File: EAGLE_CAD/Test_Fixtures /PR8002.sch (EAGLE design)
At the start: 29 parts, among them J1 M3_SCREW_POST, U1 V_REG_317SMD

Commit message: Updates to PR8002
Added RPI GPIO connections.
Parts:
- removed JP1, JP2: SMT/THJumper, SparkFun-Connectors:M02LOCK_LONGPADS
- removed TO_MCU: PINHD-1X10, adafruit:PINHD-1X10
- added LED2, LED3: (no value), adafruit:LEDCHIP-LED0805
- added R3: 1k, PR_Parts_Library:R_SMT_0805_ADAFRUIT
- added RPI_GPIO: M13X22X13, PR_Parts_Library:M13X22X13
- added U$20, U$22, U$23, U$24: C&K_PTS645, PR_Parts_Library:C&K_PTS645
- LED1: device adafruit:LED5MM -> adafruit:LEDCHIP-LED0805
- R1: value RV170SF_TAIWANA_POT_SW -> 1k; device PR_Parts_Library:RV170SF_TAIWANA_POT_SW -> PR_Parts_Library:R_SMT_0805_ADAFRUIT; MFG_PN RV170SF-43-20F-A10K - supplied by CL Labs -> (none)
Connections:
- removed net DUTPRES: TO_MCU.1, U$2.P$1
- removed net TSW: TO_MCU.4, U$9.P$1
- new net A_IN: U$17.P$1
- new net DEV_PRES: RPI_GPIO.GPIO3, U$2.P$1
- new net N$10: LED3.C, R3.2
- new net N$3: RPI_GPIO.GPIO8, U$20.P$1
- new net N$4: RPI_GPIO.GPIO12, U$23.P$1
- new net N$8: LED3.A, RPI_GPIO.GPIO23
- new net N$9: LED2.C, R1.2
- new net TACSW: RPI_GPIO.GPIO5, U$9.P$1
- net A_OUT: no longer JP1.1
- net GND: now also R1.1, R3.1, RPI_GPIO.GND, U$20.P$4, U$22.P$4, U$23.P$4, U$24.P$4; no longer R1.GND
- net N$5: now also RPI_GPIO.GPIO10, U$22.P$1; no longer JP2.1, R1.SIGNAL
- net N$6: now also RPI_GPIO.GPIO16, U$24.P$1; no longer JP1.2, R1.WIPER
- net N$7: now also LED2.A, RPI_GPIO.GPIO21; no longer JP2.2, U$17.P$1
- net SW_IN: now also RPI_GPIO.GPIO11; no longer TO_MCU.2
- net SW_OUT: now also RPI_GPIO.GPIO13; no longer TO_MCU.3
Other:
- note added: "Audio from FMIC"
- note added: "Fixture Input | Station Set Switches"
- note added: "Output from POT to Amp"
- note added: "PR8002, PR92X Test Fixture"
- note added: "Pass Fail Indication"
- note added: "RPI Connect"
- note added: "Verifies radio's LED"
- note removed: "MCU Connect"
- note removed: "NOTES: - PSU, connects via dc barrel jack to a 3.3 vreg. -MCU header connects to tactile switch; device present (ground pad), and the two poles of the switched potentiometer (when populated). -LED, connects to an external led on the test fixture. -Ext Speaker, connects to JST jack on the fixture. -Switched Pot, allows for volume control when testing SMT only boards. Uses shunt jumpers when fully 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"
- note removed: "POT"
- note removed: "PR9020 Test Fixture"
- moved on the sheet: CN1, ISP1, LED1, R2

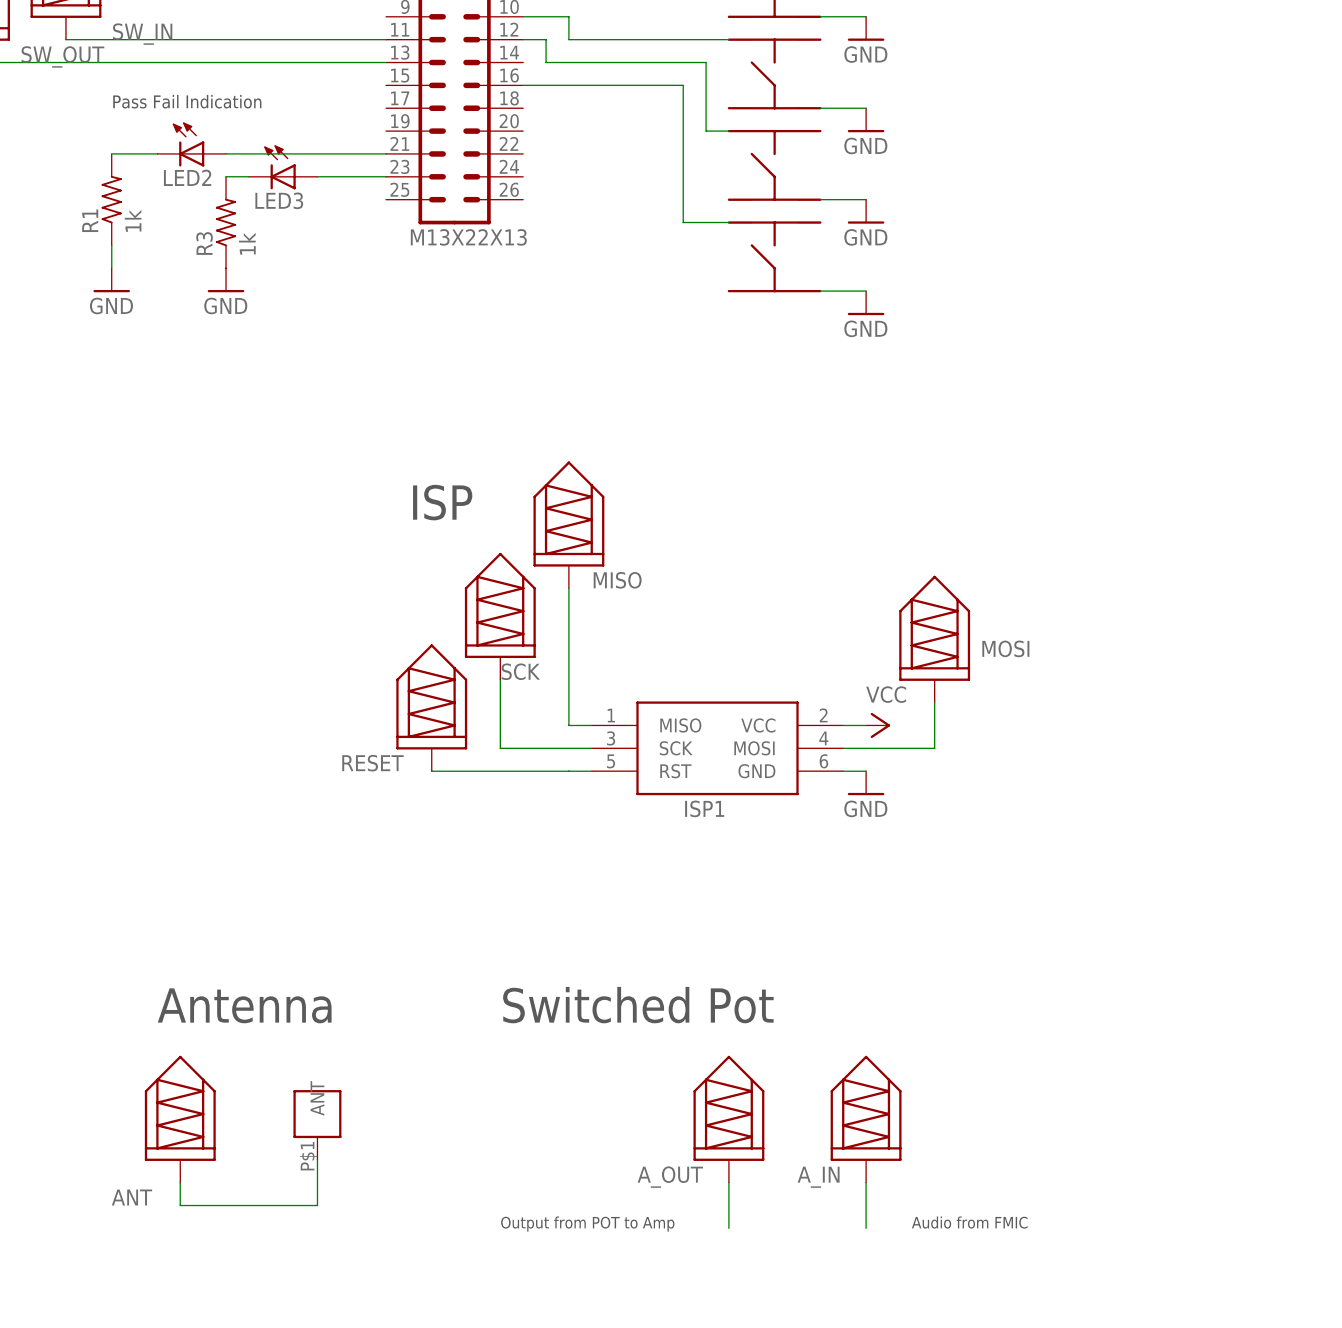
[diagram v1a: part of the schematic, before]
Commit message: PR8002 Updates
Progress on the Etest fixture schematic and layout
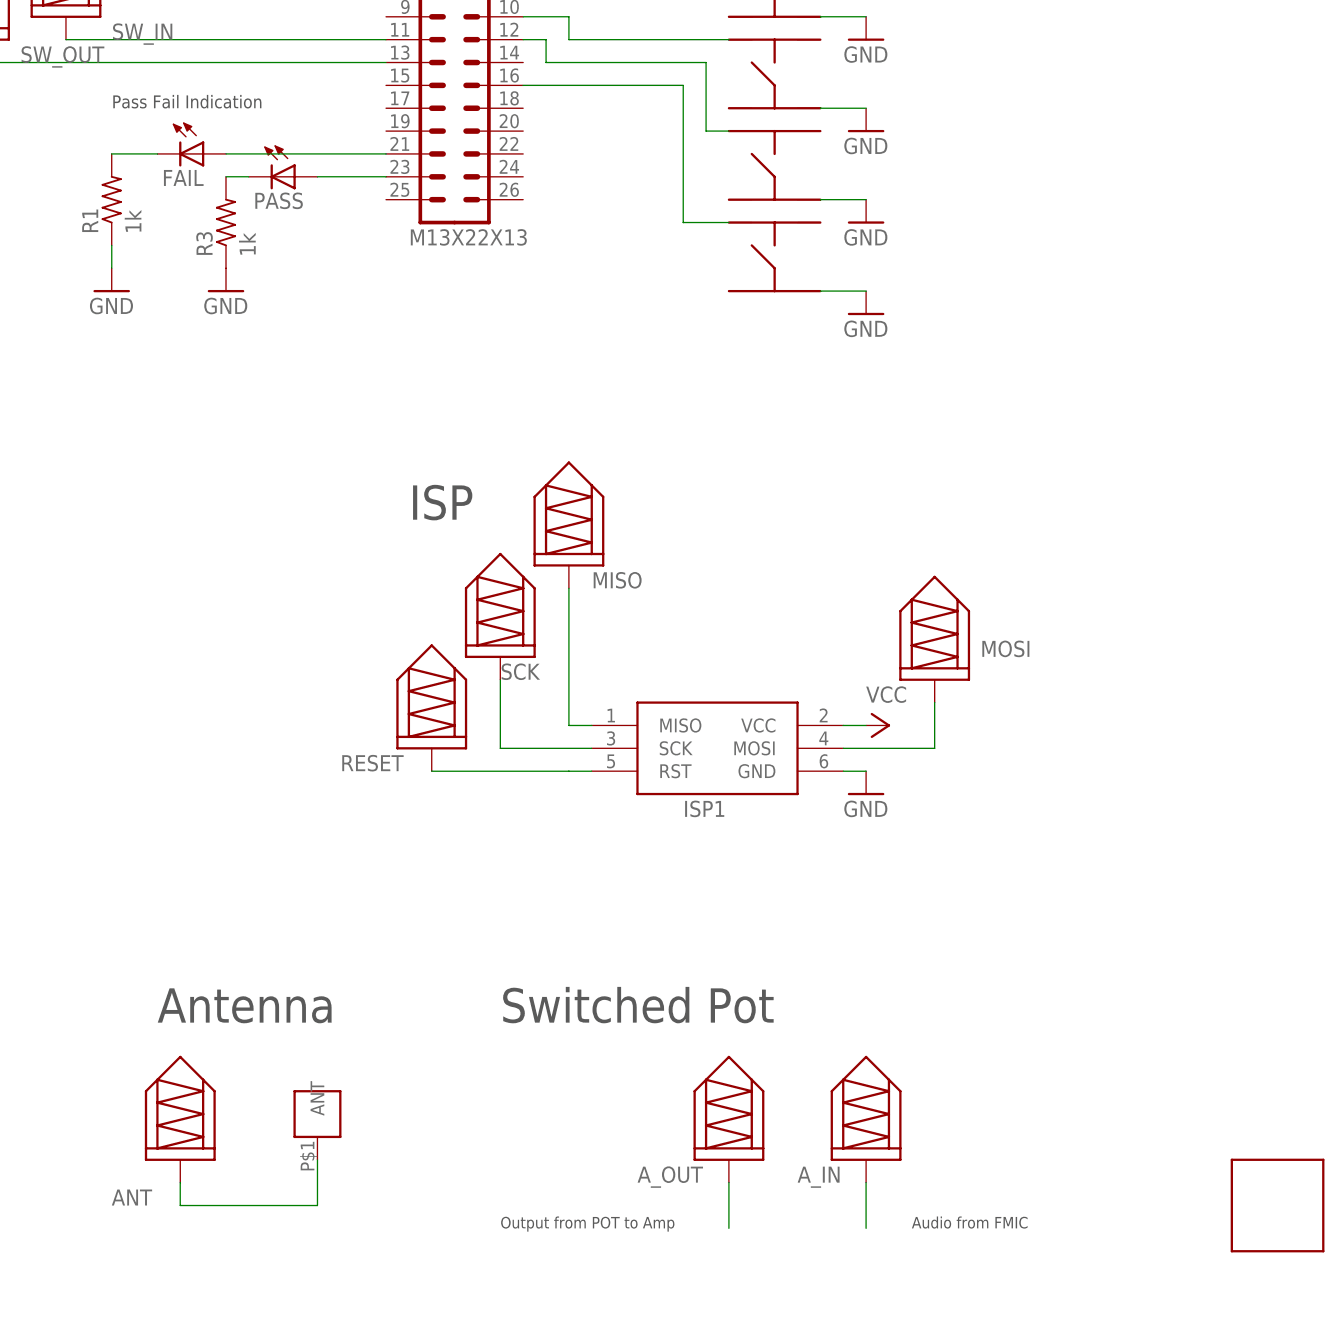
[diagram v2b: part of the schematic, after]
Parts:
- added U$25: SFUN_POCKETPROGRAMMER, PR_Parts_Library:SFUN_POCKETPROGRAMMER
- renumbered LED2 to FAIL, LED3 to PASS
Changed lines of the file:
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@@
 <part name="GND9" library="SparkFun-Aesthetics" deviceset="GND" device=""/>
 <part name="GND10" library="SparkFun-Aesthetics" deviceset="GND" device=""/>
-<part name="LED2" library="adafruit" deviceset="LED" device="CHIP-LED0805"/>
-<part name="LED3" library="adafruit" deviceset="LED" device="CHIP-LED0805"/>
+<part name="FAIL" library="adafruit" deviceset="LED" device="CHIP-LED0805"/>
+<part name="PASS" library="adafruit" deviceset="LED" device="CHIP-LED0805"/>
 <part name="R1" library="PR_Parts_Library" deviceset="R_SMT" device="_0805_ADAFRUIT" value="1k"/>
 <part name="R3" library="PR_Parts_Library" deviceset="R_SMT" device="_0805_ADAFRUIT" value="1k"/>
 <part name="GND11" library="SparkFun-Aesthetics" deviceset="GND" device=""/>
 <part name="GND12" library="SparkFun-Aesthetics" deviceset="GND" device=""/>
+<part name="U$25" library="PR_Parts_Library" deviceset="SFUN_POCKETPROGRAMMER" device=""/>
 </parts>
 <sheets>
@@
 <instance part="GND9" gate="1" x="205.74" y="106.68"/>
 <instance part="GND10" gate="1" x="205.74" y="96.52"/>
-<instance part="LED2" gate="G$1" x="132.08" y="114.3" rot="R270"/>
-<instance part="LED3" gate="G$1" x="142.24" y="111.76" rot="R270"/>
+<instance part="FAIL" gate="G$1" x="132.08" y="114.3" rot="R270"/>
+<instance part="PASS" gate="G$1" x="142.24" y="111.76" rot="R270"/>
 <instance part="R1" gate="G$1" x="121.92" y="109.22" rot="R90"/>
 <instance part="R3" gate="G$1" x="134.62" y="106.68" rot="R90"/>
 <instance part="GND11" gate="1" x="134.62" y="99.06"/>
 <instance part="GND12" gate="1" x="121.92" y="99.06"/>
+<instance part="U$25" gate="G$1" x="251.46" y="-2.54"/>
 </instances>
 <busses>
@@
 <segment>
 <pinref part="RPI_GPIO" gate="G$1" pin="GPIO21"/>
-<pinref part="LED2" gate="G$1" pin="A"/>
+<pinref part="FAIL" gate="G$1" pin="A"/>
 <wire x1="134.62" y1="114.3" x2="152.4" y2="114.3" width="0.1524" layer="91"/>
 </segment>
@@
 <segment>
 <pinref part="RPI_GPIO" gate="G$1" pin="GPIO23"/>
-<pinref part="LED3" gate="G$1" pin="A"/>
+<pinref part="PASS" gate="G$1" pin="A"/>
 <wire x1="144.78" y1="111.76" x2="152.4" y2="111.76" width="0.1524" layer="91"/>
 </segment>
@@
 <net name="N$9" class="0">
 <segment>
-<pinref part="LED2" gate="G$1" pin="C"/>
+<pinref part="FAIL" gate="G$1" pin="C"/>
 <pinref part="R1" gate="G$1" pin="2"/>
 <wire x1="121.92" y1="114.3" x2="127" y2="114.3" width="0.1524" layer="91"/>
@@
 <net name="N$10" class="0">
 <segment>
-<pinref part="LED3" gate="G$1" pin="C"/>
+<pinref part="PASS" gate="G$1" pin="C"/>
 <pinref part="R3" gate="G$1" pin="2"/>
 <wire x1="134.62" y1="111.76" x2="137.16" y2="111.76" width="0.1524" layer="91"/>

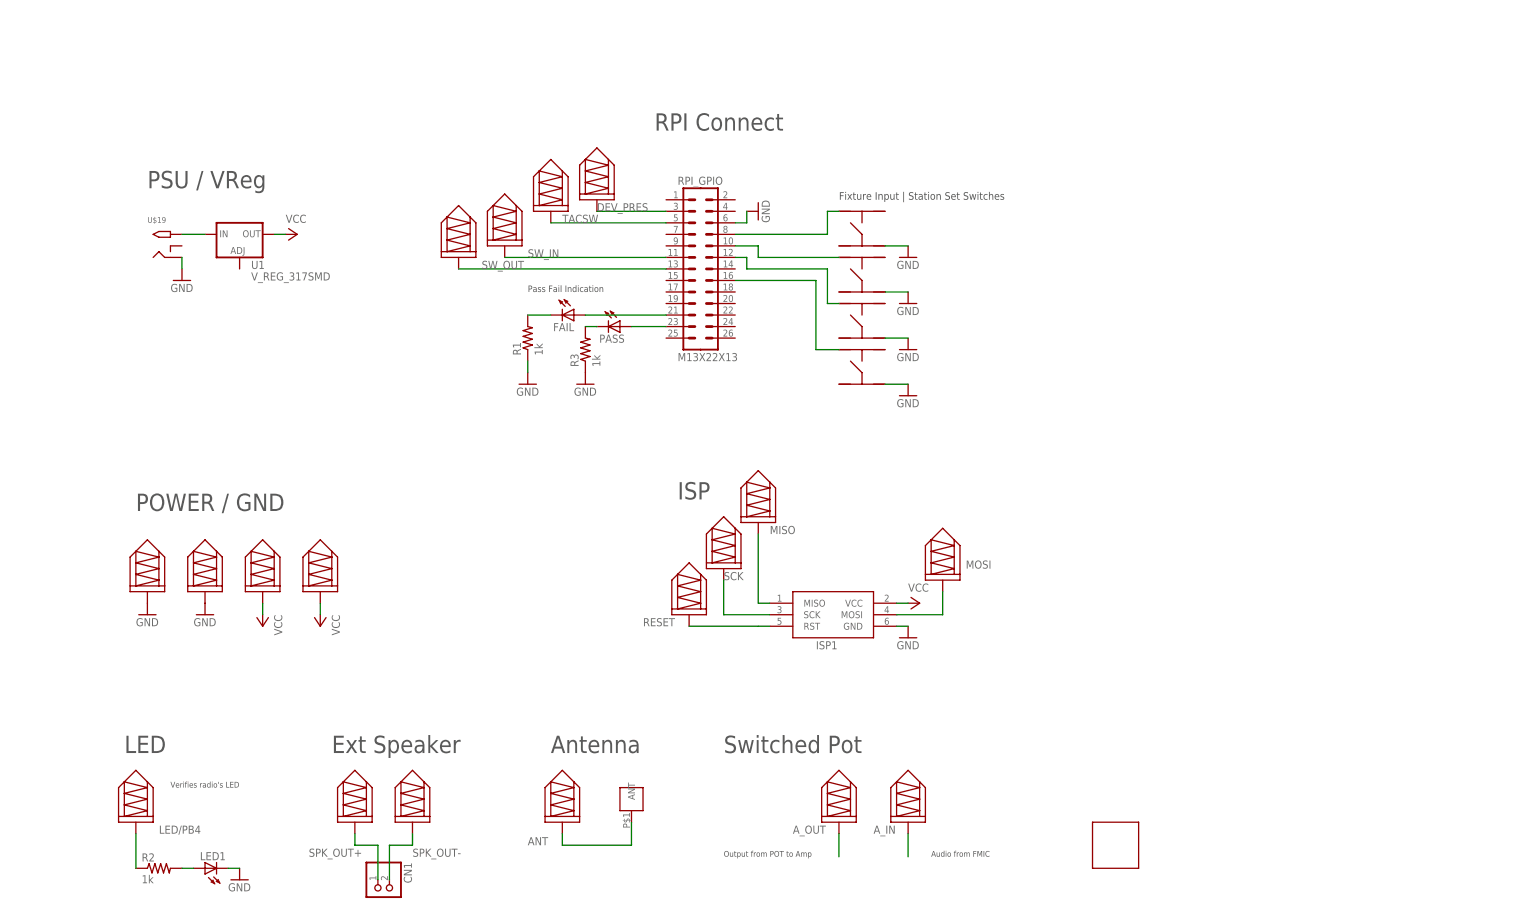
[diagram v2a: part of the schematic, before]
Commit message: PR8002 Updates
Added current monitoring and Vreg per Andy’s notes.
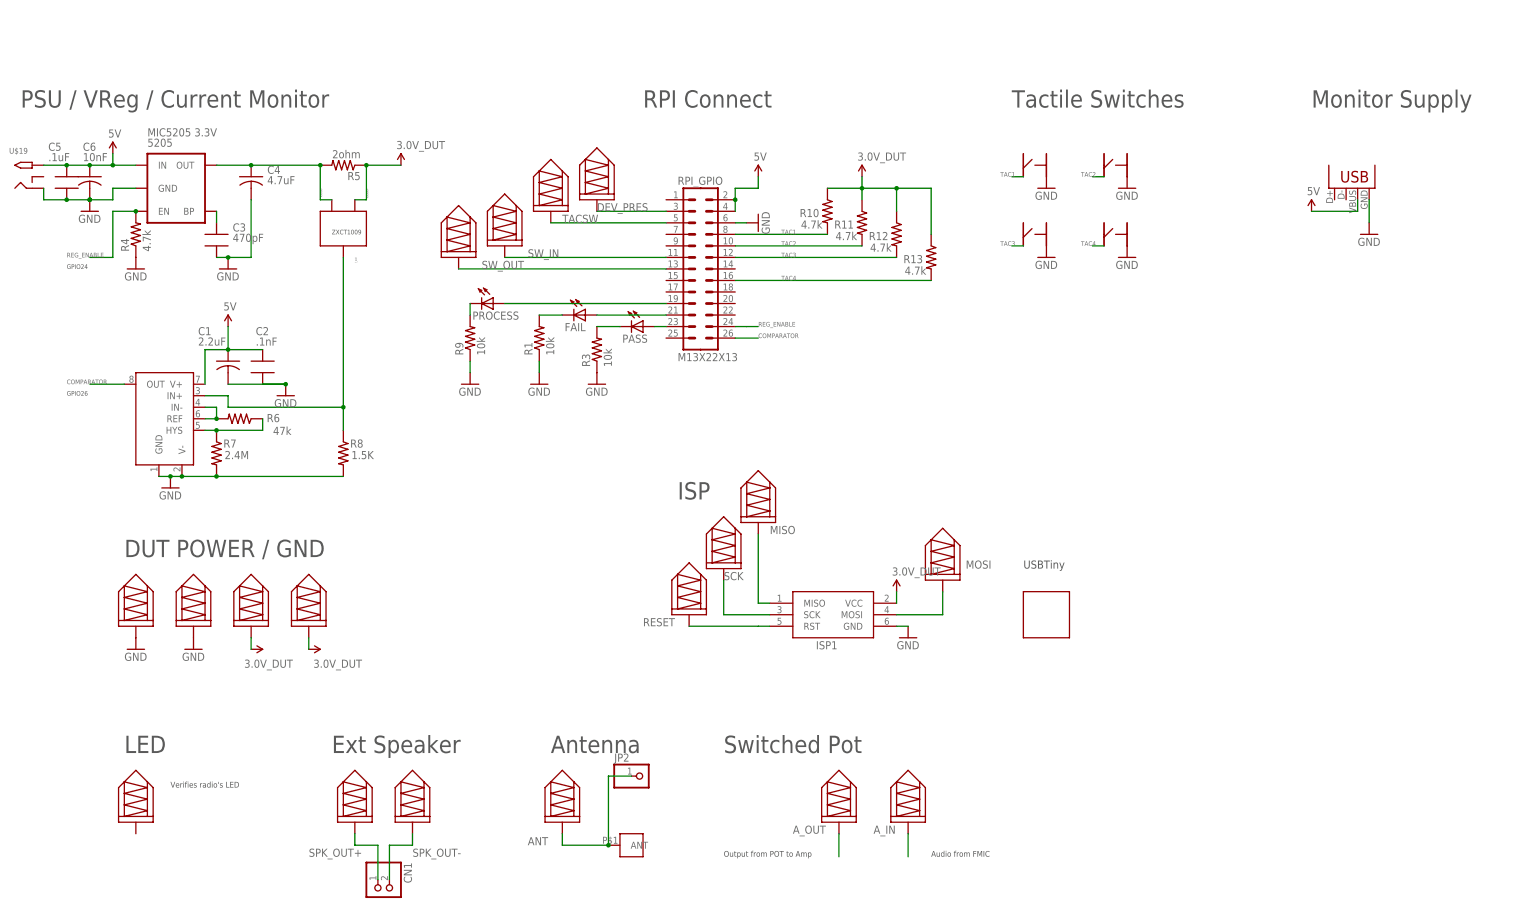
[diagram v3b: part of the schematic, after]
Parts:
- removed LED1: (no value), adafruit:LEDCHIP-LED0805
- removed R2: 1k, PR_Parts_Library:R_SMT_0805_ADAFRUIT
- removed U1: V_REG_317SMD, SparkFun-PowerIC:V_REG_317SMD
- added 5205: MIC5205 3.3V, SparkFun-PowerIC:V_REG_MIC52193.3V
- added C1: 2.2uF, adafruit:C-USC0805
- added C2: .1nF, PR_Parts_Library:C_SMT_0805_ADAFRUIT
- added C3: 470pF, PR_Parts_Library:C_SMT_0805_ADAFRUIT
- added C4: 4.7uF, adafruit:C-USC0805
- added C5: .1uF, PR_Parts_Library:C_SMT_0805_ADAFRUIT
- added C6: 10nF, adafruit:C-USC0805
- added JP1: USB-B, SparkFun-Connectors:USBPTH
- added JP2: (no value), adafruit:PINHD-1X1
- added PROCESS: (no value), adafruit:LEDCHIP-LED0805
- added R10, R11, R12, R13, R4: 4.7k, PR_Parts_Library:R_SMT_0805_ADAFRUIT
- added R5: 2ohm, PR_Parts_Library:R_SMT_0805_ADAFRUIT
- added R6: 47k, PR_Parts_Library:R_SMT_0805_ADAFRUIT
- added R7: 2.4M, PR_Parts_Library:R_SMT_0805_ADAFRUIT
- added R8: 1.5K, PR_Parts_Library:R_SMT_0805_ADAFRUIT
- added R9: 10k, PR_Parts_Library:R_SMT_0805_ADAFRUIT
- added TSM931: TSM931, PR_Parts_Library:TSM931
- added ZXCT: ZXCT1009, PR_Parts_Library:ZXCT1009
- R1, R3: value 1k -> 10k
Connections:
- removed net LED/PB4: R2.1, U$10.P$1
- removed net N$2: LED1.A, R2.2
- removed net N$3: RPI_GPIO.GPIO8, U$20.P$1
- removed net N$4: RPI_GPIO.GPIO12, U$23.P$1
- removed net N$5: RPI_GPIO.GPIO10, U$22.P$1
- removed net N$6: RPI_GPIO.GPIO16, U$24.P$1
- removed net VCC: ISP1.VCC, U$5.P$1, U$6.P$1, U1.OUT
- new net 3.3V: ISP1.VCC, R10.1, R11.1, R12.1, R13.1, R5.1, U$5.P$1, U$6.P$1, ZXCT.VSENSE+
- new net 5V: 5205.IN, C1.1, C2.1, C5.1, C6.1, JP1.VBUS, RPI_GPIO.5V, RPI_GPIO.DNC1, TSM931.V+, U$19.TIP
- new net COMPARATOR: RPI_GPIO.GPIO26, TSM931.OUT
- new net N$12: R8.1, TSM931.IN+, ZXCT.IOUT
- new net N$13: 5205.BP, C3.1
- new net N$14: 5205.OUT, C4.1, R5.2, ZXCT.VSENSE-
- new net N$15: R6.1, R7.1, TSM931.HYS
- new net N$16: PROCESS.A, RPI_GPIO.GPIO19
- new net N$17: PROCESS.C, R9.2
- new net REG_ENABLE: 5205.EN, R4.2, RPI_GPIO.GPIO24
- new net TAC1: R10.2, RPI_GPIO.GPIO8, U$20.P$4
- new net TAC2: R11.2, RPI_GPIO.GPIO10, U$23.P$4
- new net TAC3: R12.2, RPI_GPIO.GPIO12, U$22.P$4
- new net TAC4: R13.2, RPI_GPIO.GPIO16, U$24.P$4
- net ANT: now also JP2.1
- net GND: now also 5205.GND, C1.2, C2.2, C3.2, C4.2, C5.2, C6.2, JP1.GND, R4.1, R7.2, R8.2, R9.1, TSM931.GND, TSM931.V-, U$20.P$2, U$22.P$2, U$23.P$2, U$24.P$2; no longer LED1.C, U$20.P$4, U$22.P$4, U$23.P$4, U$24.P$4
- net N$1: now also R6.2, TSM931.IN-, TSM931.REF; no longer U$19.TIP, U1.IN
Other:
- note added: "DUT POWER / GND"
- note added: "GPIO24"
- note added: "GPIO26"
- note added: "Monitor Supply"
- note added: "PSU / VReg / Current Monitor"
- note added: "Tactile Switches"
- note added: "USBTiny"
- note added: "ZXCT1009"
- note removed: "Fixture Input | Station Set Switches"
- note removed: "POWER / GND"
- note removed: "PSU / VReg"
- note removed: "Pass Fail Indication"
- moved on the sheet: FAIL, PASS, R1, R3, U$19
